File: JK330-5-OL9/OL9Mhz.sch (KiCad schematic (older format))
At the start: 46 parts, among them K1 CONN_3, K2 CONN_2, K3 COLONETTE, K4 COLONETTE, K5 COLONETTE, K6 COLONETTE, P1 U.FL, P2 BNC, Q1 BSN20, U1 BF996, U2 BF996, X1 9Mhz, X2 9Mhz

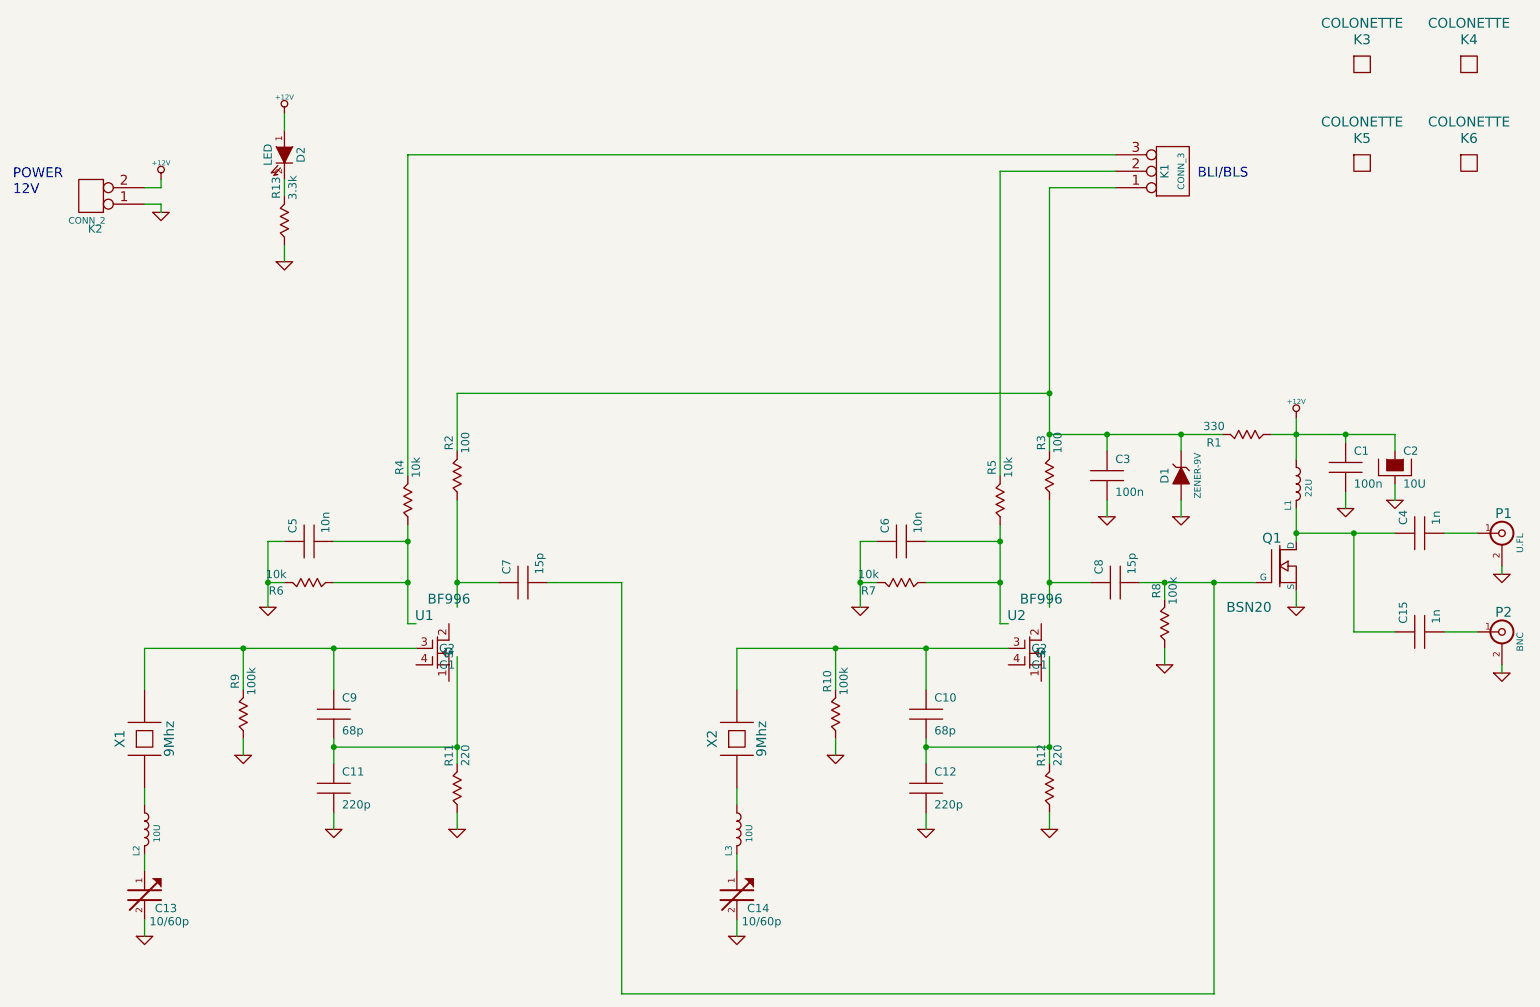
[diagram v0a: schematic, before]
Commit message: correction bf996 schema
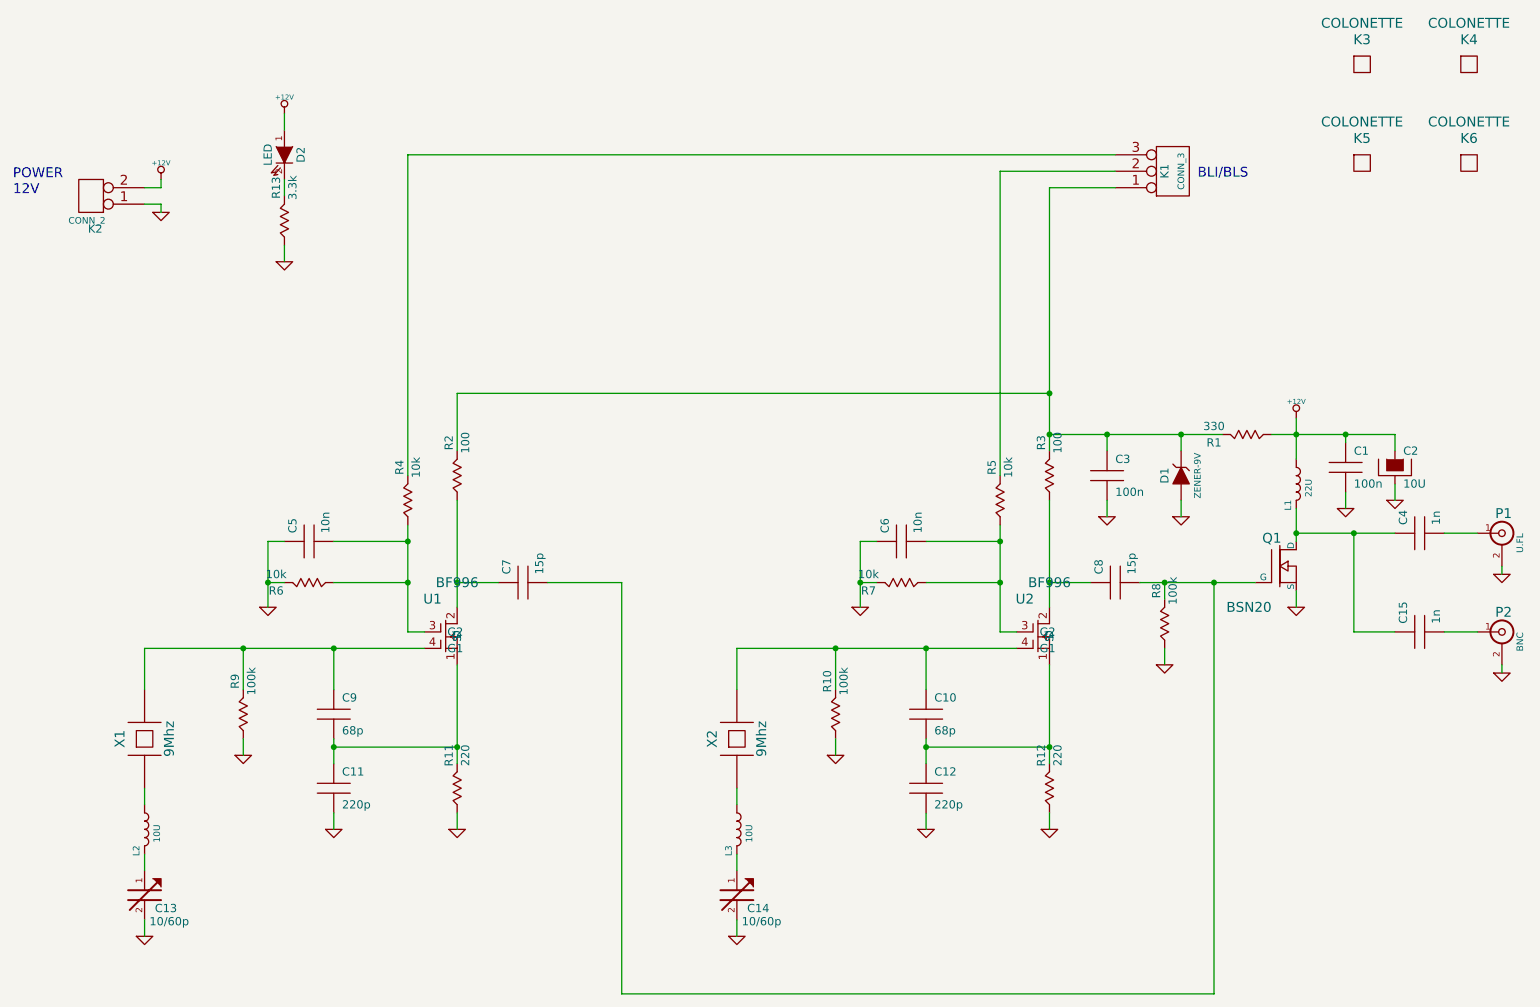
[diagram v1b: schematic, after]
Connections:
- wire segments 86 -> 113
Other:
- moved on the sheet: U1, U2
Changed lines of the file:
@@
-EESchema Schematic File Version 2  date 2013-03-30 15:42:45
+EESchema Schematic File Version 2  date 28/04/2013 22:42:08
 LIBS:power
 LIBS:CEN-SCHEMA
-LIBS:device
-LIBS:transistors
-LIBS:linear
 LIBS:OL9Mhz-cache
 EELAYER 27 0
@@
 Sheet 1 1
 Title "JK330-Oscillateur Local 9Mhz"
-Date "30 mar 2013"
+Date "28 apr 2013"
 Rev "V0-10"
 Comp "F4DEB"
@@
 L BF996 U2
 U 1 1 514F6B5B
-P 7600 4400
-F 0 "U2" H 7500 4500 60  0000 C CNN
-F 1 "BF996" H 7650 4600 60  0000 C CNN
-F 2 "" H 7600 4400 60  0000 C CNN
-F 3 "" H 7600 4400 60  0000 C CNN
-	1    7600 4400
+P 7650 4300
+F 0 "U2" H 7550 4400 60  0000 C CNN
+F 1 "BF996" H 7700 4500 60  0000 C CNN
+F 2 "" H 7650 4300 60  0000 C CNN
+F 3 "" H 7650 4300 60  0000 C CNN
+	1    7650 4300
 	1    0    0    -1
 $EndComp
@@
 	5800 4500 5800 4750
 Wire Wire Line
-	7700 4550 7700 5200
-Wire Wire Line
-	6950 5050 6950 5200
+	7700 4600 7700 5100
+Wire Wire Line
+	7700 5100 7700 5200
+Wire Wire Line
+	6950 5050 6950 5100
+Wire Wire Line
+	6950 5100 6950 5200
 Wire Wire Line
 	6950 5100 7700 5100
@@
 Connection ~ 6950 5100
 Wire Wire Line
-	5800 4500 7450 4500
+	5800 4500 6400 4500
+Wire Wire Line
+	6400 4500 6950 4500
+Wire Wire Line
+	6950 4500 7500 4500
 Wire Wire Line
 	6400 4750 6400 4500
@@
 $EndComp
 Wire Wire Line
-	7400 3750 7400 4350
+	7400 3750 7400 3850
+Wire Wire Line
+	7400 3850 7400 4100
+Wire Wire Line
+	7400 4100 7400 4400
 Wire Wire Line
 	6950 3850 7400 3850
@@
 	6650 3850 6550 3850
 Wire Wire Line
-	6550 3850 6550 4250
+	6550 3850 6550 4100
+Wire Wire Line
+	6550 4100 6550 4250
 Wire Wire Line
 	6650 4100 6550 4100
@@
 $EndComp
 Wire Wire Line
-	7700 3600 7700 4250
-Wire Wire Line
-	7700 1700 7700 3300
-Wire Wire Line
-	7700 3200 8750 3200
+	7700 3600 7700 4100
+Wire Wire Line
+	7700 4100 7700 4250
+Wire Wire Line
+	7700 1700 7700 2950
+Wire Wire Line
+	7700 2950 7700 3200
+Wire Wire Line
+	7700 3200 7700 3300
+Wire Wire Line
+	7700 3200 8050 3200
+Wire Wire Line
+	8050 3200 8500 3200
+Wire Wire Line
+	8500 3200 8750 3200
 Connection ~ 7700 3200
 Wire Wire Line
@@
 $EndComp
 Wire Wire Line
-	9050 3200 9800 3200
-Wire Wire Line
-	9200 3100 9200 3350
+	9050 3200 9200 3200
+Wire Wire Line
+	9200 3200 9500 3200
+Wire Wire Line
+	9500 3200 9800 3200
+Wire Wire Line
+	9200 3100 9200 3200
+Wire Wire Line
+	9200 3200 9200 3350
 $Comp
 L +12V #PWR08
@@
 Connection ~ 7700 4100
 Wire Wire Line
-	8250 4100 8950 4100
+	8250 4100 8400 4100
+Wire Wire Line
+	8400 4100 8700 4100
+Wire Wire Line
+	8700 4100 8950 4100
 Wire Wire Line
 	8400 4200 8400 4100
@@
 L BF996 U1
 U 1 1 514F715C
-P 4000 4400
-F 0 "U1" H 3900 4500 60  0000 C CNN
-F 1 "BF996" H 4050 4600 60  0000 C CNN
-F 2 "" H 4000 4400 60  0000 C CNN
-F 3 "" H 4000 4400 60  0000 C CNN
-	1    4000 4400
+P 4050 4300
+F 0 "U1" H 3950 4400 60  0000 C CNN
+F 1 "BF996" H 4100 4500 60  0000 C CNN
+F 2 "" H 4050 4300 60  0000 C CNN
+F 3 "" H 4050 4300 60  0000 C CNN
+	1    4050 4300
 	1    0    0    -1
 $EndComp
@@
 	2200 4500 2200 4750
 Wire Wire Line
-	4100 4550 4100 5200
-Wire Wire Line
-	3350 5050 3350 5200
+	4100 4600 4100 5100
+Wire Wire Line
+	4100 5100 4100 5200
+Wire Wire Line
+	3350 5050 3350 5100
+Wire Wire Line
+	3350 5100 3350 5200
 Wire Wire Line
 	3350 5100 4100 5100
@@
 Connection ~ 3350 5100
 Wire Wire Line
-	2200 4500 3850 4500
+	2200 4500 2800 4500
+Wire Wire Line
+	2800 4500 3350 4500
+Wire Wire Line
+	3350 4500 3900 4500
 Wire Wire Line
 	2800 4750 2800 4500
@@
 $EndComp
 Wire Wire Line
-	3800 3750 3800 4350
+	3800 3750 3800 3850
+Wire Wire Line
+	3800 3850 3800 4100
+Wire Wire Line
+	3800 4100 3800 4400
 Wire Wire Line
 	3350 3850 3800 3850
@@
 	3050 3850 2950 3850
 Wire Wire Line
-	2950 3850 2950 4250
+	2950 3850 2950 4100
+Wire Wire Line
+	2950 4100 2950 4250
 Wire Wire Line
 	3050 4100 2950 4100
@@
 $EndComp
 Wire Wire Line
-	4100 3600 4100 4250
+	4100 3600 4100 4100
+Wire Wire Line
+	4100 4100 4100 4250
 $Comp
 L C C7
@@
 Connection ~ 9200 3200
 Wire Wire Line
-	9200 3650 9200 3850
+	9200 3650 9200 3800
+Wire Wire Line
+	9200 3800 9200 3850
 Wire Wire Line
 	9200 4150 9200 4250
@@
 $EndComp
 Wire Wire Line
-	9200 3800 9800 3800
+	9200 3800 9550 3800
+Wire Wire Line
+	9550 3800 9800 3800
 Connection ~ 9200 3800
 $Comp
@@
 POWER\n12V
 Wire Wire Line
-	3800 4350 3850 4350
-Wire Wire Line
-	7400 4350 7450 4350
+	3800 4400 3900 4400
+Wire Wire Line
+	7400 4400 7500 4400
 $Comp
 L R R13

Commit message: MAJ
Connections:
- net at C6.2, R7.2, U2.3 (G2): no longer R5.2
- net at R5.1: no longer K1.2 (PM)
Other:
- moved on the sheet: R5
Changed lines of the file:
@@
-EESchema Schematic File Version 2  date 28/04/2013 22:42:08
+EESchema Schematic File Version 2
 LIBS:power
 LIBS:CEN-SCHEMA
@@
 Sheet 1 1
 Title "JK330-Oscillateur Local 9Mhz"
-Date "28 apr 2013"
+Date "28 dec 2013"
 Rev "V0-10"
 Comp "F4DEB"
@@
 U 1 1 514F661E
 P 5800 5750
-F 0 "L3" V 5750 5770 40  0000 C CNN
+F 0 "L3" V 5750 5900 40  0000 C CNN
 F 1 "10U" V 5875 5875 40  0000 C CNN
 F 2 "" H 5800 5750 60  0000 C CNN
@@
 U 1 1 514F6641
 P 6400 4800
-F 0 "R10" V 6350 4900 50  0000 C CNN
-F 1 "100k" V 6450 4900 50  0000 C CNN
+F 0 "R10" V 6350 4700 50  0000 C CNN
+F 1 "100k" V 6450 4700 50  0000 C CNN
 F 2 "" H 6400 4800 60  0000 C CNN
 F 3 "" H 6400 4800 60  0000 C CNN
@@
 U 1 1 514F6669
 P 7700 5250
-F 0 "R12" V 7650 5350 50  0000 C CNN
-F 1 "220" V 7750 5350 50  0000 C CNN
+F 0 "R12" V 7650 5150 50  0000 C CNN
+F 1 "220" V 7750 5150 50  0000 C CNN
 F 2 "" H 7700 5250 60  0000 C CNN
 F 3 "" H 7700 5250 60  0000 C CNN
@@
 U 1 1 514F6B5B
 P 7650 4300
-F 0 "U2" H 7550 4400 60  0000 C CNN
-F 1 "BF996" H 7700 4500 60  0000 C CNN
+F 0 "U2" H 7850 4300 60  0000 C CNN
+F 1 "BF996" H 7900 4150 60  0000 C CNN
 F 2 "" H 7650 4300 60  0000 C CNN
 F 3 "" H 7650 4300 60  0000 C CNN
@@
 U 1 1 514F6C79
 P 6700 4100
-F 0 "R7" V 6650 4200 50  0000 C CNN
-F 1 "10k" V 6750 4200 50  0000 C CNN
+F 0 "R7" V 6650 4000 50  0000 C CNN
+F 1 "10k" V 6750 4000 50  0000 C CNN
 F 2 "" H 6700 4100 60  0000 C CNN
 F 3 "" H 6700 4100 60  0000 C CNN
@@
 U 1 1 514F6C88
 P 6800 3850
-F 0 "C6" H 6850 3950 50  0000 L CNN
-F 1 "10n" H 6850 3750 50  0000 L CNN
+F 0 "C6" V 6850 3900 50  0000 L CNN
+F 1 "10n" V 6850 3650 50  0000 L CNN
 F 2 "" H 6800 3850 60  0000 C CNN
 F 3 "" H 6800 3850 60  0000 C CNN
@@
 L R R5
 U 1 1 514F6C97
-P 7400 3500
-F 0 "R5" V 7350 3600 50  0000 C CNN
-F 1 "10k" V 7450 3600 50  0000 C CNN
-F 2 "" H 7400 3500 60  0000 C CNN
-F 3 "" H 7400 3500 60  0000 C CNN
-	1    7400 3500
+P 7400 3550
+F 0 "R5" V 7350 3450 50  0000 C CNN
+F 1 "10k" V 7450 3450 50  0000 C CNN
+F 2 "" H 7400 3550 60  0000 C CNN
+F 3 "" H 7400 3550 60  0000 C CNN
+	1    7400 3550
 	1    0    0    -1
 $EndComp
@@
 U 1 1 514F6DB7
 P 7700 3350
-F 0 "R3" V 7650 3450 50  0000 C CNN
-F 1 "100" V 7750 3450 50  0000 C CNN
+F 0 "R3" V 7650 3250 50  0000 C CNN
+F 1 "100" V 7750 3250 50  0000 C CNN
 F 2 "" H 7700 3350 60  0000 C CNN
 F 3 "" H 7700 3350 60  0000 C CNN
@@
 U 1 1 514F6DEA
 P 8800 3200
-F 0 "R1" V 8750 3300 50  0000 C CNN
-F 1 "330" V 8850 3300 50  0000 C CNN
+F 0 "R1" V 8750 3100 50  0000 C CNN
+F 1 "330" V 8850 3100 50  0000 C CNN
 F 2 "" H 8800 3200 60  0000 C CNN
 F 3 "" H 8800 3200 60  0000 C CNN
@@
 U 1 1 514F6FBA
 P 8100 4100
-F 0 "C8" H 8150 4200 50  0000 L CNN
-F 1 "15p" H 8150 4000 50  0000 L CNN
+F 0 "C8" V 8200 4200 50  0000 L CNN
+F 1 "15p" V 8200 3900 50  0000 L CNN
 F 2 "" H 8100 4100 60  0000 C CNN
 F 3 "" H 8100 4100 60  0000 C CNN
@@
 U 1 1 514F6FDF
 P 8400 4250
-F 0 "R8" V 8350 4350 50  0000 C CNN
-F 1 "100k" V 8450 4350 50  0000 C CNN
+F 0 "R8" V 8350 4150 50  0000 C CNN
+F 1 "100k" V 8450 4150 50  0000 C CNN
 F 2 "" H 8400 4250 60  0000 C CNN
 F 3 "" H 8400 4250 60  0000 C CNN
@@
 U 1 1 514F7144
 P 2200 5750
-F 0 "L2" V 2150 5770 40  0000 C CNN
+F 0 "L2" V 2150 5900 40  0000 C CNN
 F 1 "10U" V 2275 5875 40  0000 C CNN
 F 2 "" H 2200 5750 60  0000 C CNN
@@
 U 1 1 514F714A
 P 2800 4800
-F 0 "R9" V 2750 4900 50  0000 C CNN
-F 1 "100k" V 2850 4900 50  0000 C CNN
+F 0 "R9" V 2750 4700 50  0000 C CNN
+F 1 "100k" V 2850 4700 50  0000 C CNN
 F 2 "" H 2800 4800 60  0000 C CNN
 F 3 "" H 2800 4800 60  0000 C CNN
@@
 U 1 1 514F7156
 P 4100 5250
-F 0 "R11" V 4050 5350 50  0000 C CNN
-F 1 "220" V 4150 5350 50  0000 C CNN
+F 0 "R11" V 4050 5150 50  0000 C CNN
+F 1 "220" V 4150 5150 50  0000 C CNN
 F 2 "" H 4100 5250 60  0000 C CNN
 F 3 "" H 4100 5250 60  0000 C CNN
@@
 U 1 1 514F715C
 P 4050 4300
-F 0 "U1" H 3950 4400 60  0000 C CNN
-F 1 "BF996" H 4100 4500 60  0000 C CNN
+F 0 "U1" H 4250 4200 60  0000 C CNN
+F 1 "BF996" H 4300 4100 60  0000 C CNN
 F 2 "" H 4050 4300 60  0000 C CNN
 F 3 "" H 4050 4300 60  0000 C CNN
@@
 U 1 1 514F718B
 P 3100 4100
-F 0 "R6" V 3050 4200 50  0000 C CNN
-F 1 "10k" V 3150 4200 50  0000 C CNN
+F 0 "R6" V 3050 4050 50  0000 C CNN
+F 1 "10k" V 3150 4050 50  0000 C CNN
 F 2 "" H 3100 4100 60  0000 C CNN
 F 3 "" H 3100 4100 60  0000 C CNN
@@
 U 1 1 514F7191
 P 3200 3850
-F 0 "C5" H 3250 3950 50  0000 L CNN
-F 1 "10n" H 3250 3750 50  0000 L CNN
+F 0 "C5" V 3300 3900 50  0000 L CNN
+F 1 "10n" V 3300 3650 50  0000 L CNN
 F 2 "" H 3200 3850 60  0000 C CNN
 F 3 "" H 3200 3850 60  0000 C CNN
@@
 U 1 1 514F7197
 P 3800 3500
-F 0 "R4" V 3750 3600 50  0000 C CNN
-F 1 "10k" V 3850 3600 50  0000 C CNN
+F 0 "R4" V 3750 3400 50  0000 C CNN
+F 1 "10k" V 3850 3400 50  0000 C CNN
 F 2 "" H 3800 3500 60  0000 C CNN
 F 3 "" H 3800 3500 60  0000 C CNN
@@
 U 1 1 514F71AE
 P 4100 3350
-F 0 "R2" V 4050 3450 50  0000 C CNN
-F 1 "100" V 4150 3450 50  0000 C CNN
+F 0 "R2" V 4050 3250 50  0000 C CNN
+F 1 "100" V 4150 3250 50  0000 C CNN
 F 2 "" H 4100 3350 60  0000 C CNN
 F 3 "" H 4100 3350 60  0000 C CNN
@@
 U 1 1 514F71E5
 P 4500 4100
-F 0 "C7" H 4550 4200 50  0000 L CNN
-F 1 "15p" H 4550 4000 50  0000 L CNN
+F 0 "C7" V 4600 4150 50  0000 L CNN
+F 1 "15p" V 4600 3900 50  0000 L CNN
 F 2 "" H 4500 4100 60  0000 C CNN
 F 3 "" H 4500 4100 60  0000 C CNN
@@
 U 1 1 514F74EF
 P 9200 3650
-F 0 "L1" V 9150 3670 40  0000 C CNN
+F 0 "L1" V 9150 3800 40  0000 C CNN
 F 1 "22U" V 9275 3775 40  0000 C CNN
 F 2 "" H 9200 3650 60  0000 C CNN
@@
 U 1 1 514F7801
 P 9950 3800
-F 0 "C4" H 10000 3900 50  0000 L CNN
-F 1 "1n" H 10000 3700 50  0000 L CNN
+F 0 "C4" V 10000 3900 50  0000 L CNN
+F 1 "1n" V 10000 3650 50  0000 L CNN
 F 2 "" H 9950 3800 60  0000 C CNN
 F 3 "" H 9950 3800 60  0000 C CNN
@@
 U 1 1 514F8E93
 P 3050 1800
-F 0 "R13" V 3000 1900 50  0000 C CNN
-F 1 "3.3k" V 3100 1900 50  0000 C CNN
+F 0 "R13" V 3000 1700 50  0000 C CNN
+F 1 "3.3k" V 3100 1700 50  0000 C CNN
 F 2 "~" H 3050 1800 60  0000 C CNN
 F 3 "~" H 3050 1800 60  0000 C CNN
@@
 U 1 1 5156F305
 P 9950 4400
-F 0 "C15" H 10000 4500 50  0000 L CNN
-F 1 "1n" H 10000 4300 50  0000 L CNN
+F 0 "C15" V 10000 4500 50  0000 L CNN
+F 1 "1n" V 10000 4250 50  0000 L CNN
 F 2 "~" H 9950 4400 60  0000 C CNN
 F 3 "~" H 9950 4400 60  0000 C CNN
